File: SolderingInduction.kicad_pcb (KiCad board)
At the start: 4 copper layers, 69 x 37.6 mm, 52 parts, among them J1 MC-307, J3 RBP_GPIO_CONN, SW1 SW_Push, SW2 SW_Push, SW3 SW_Push, SW4 SW_Push, SW5 SW_Push, SW6 SW_Push, SW7 SW_Push, SW8 SW_Push, U1 SPX2920M3-3.3_SOT223, U3 W25Q32JVZP, U4 RP2040, Y1 X322512MMB4SI

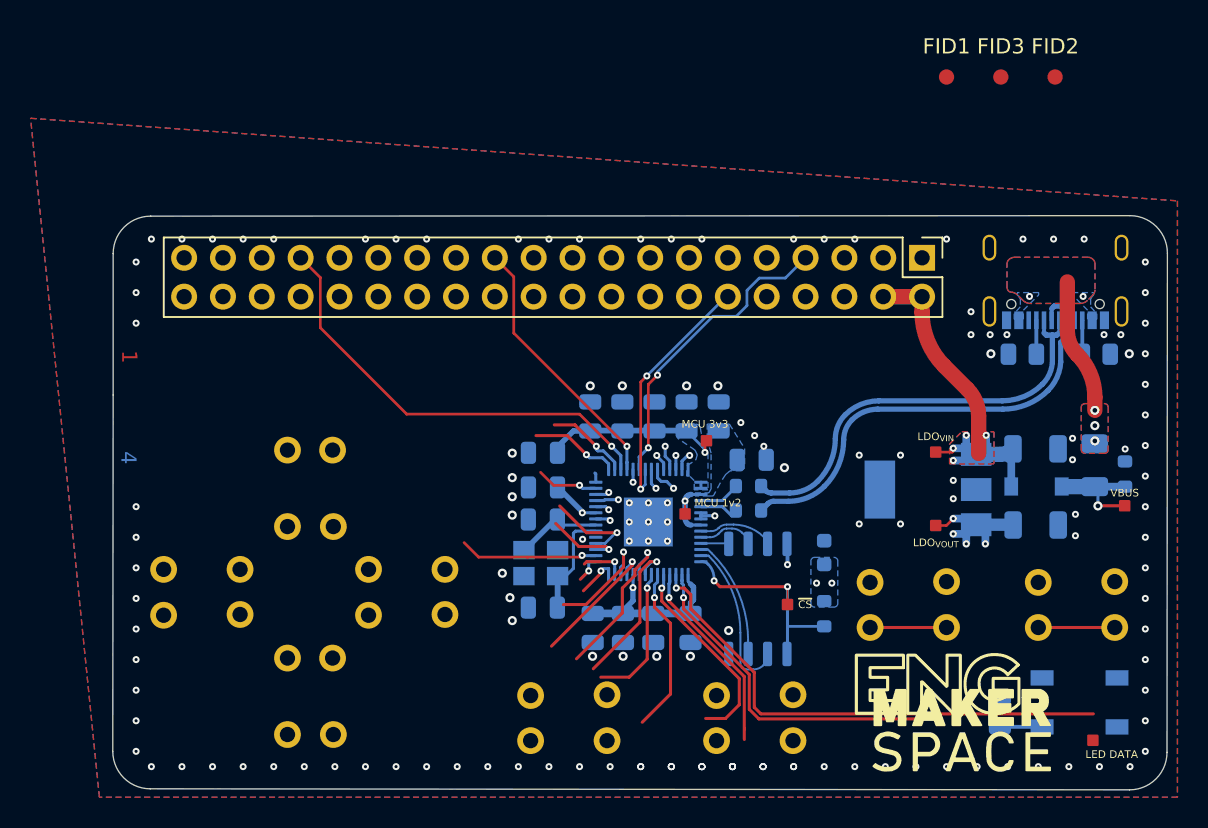
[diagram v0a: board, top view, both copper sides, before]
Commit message: Rough layout run to pinheader
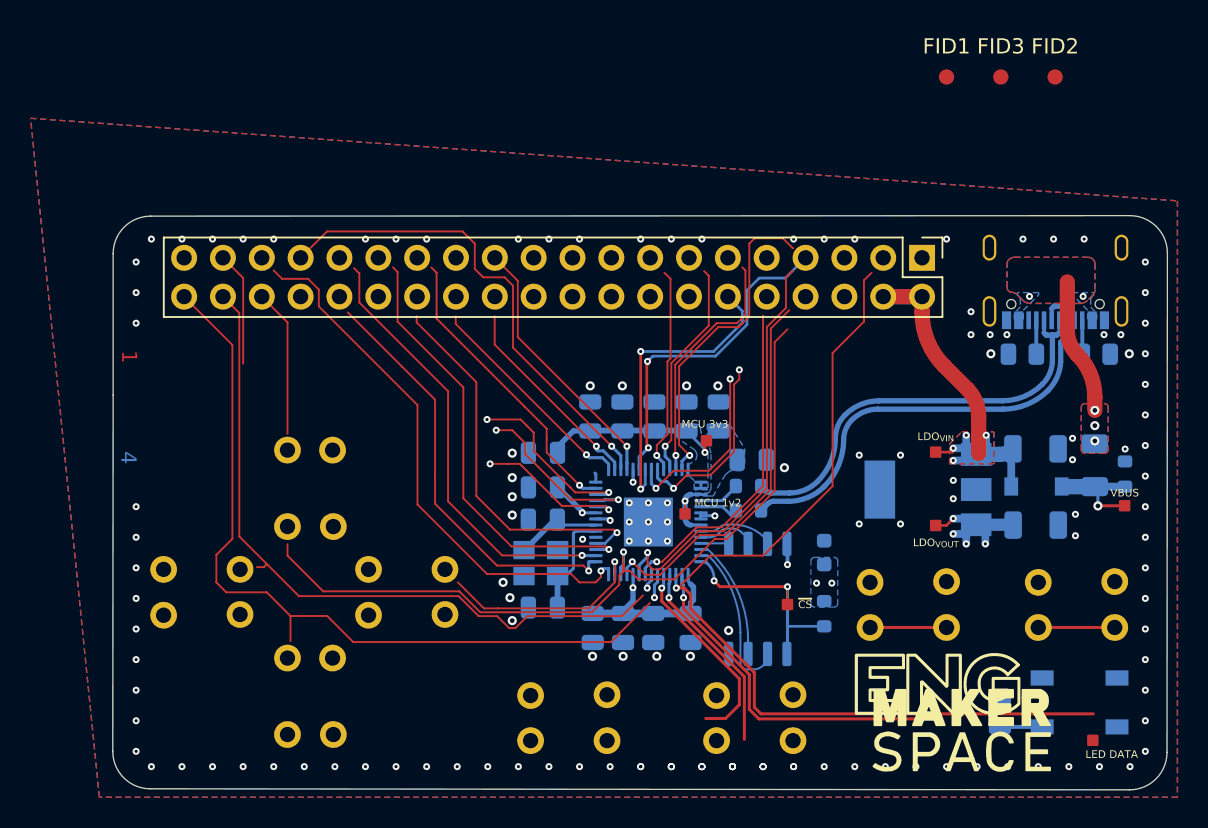
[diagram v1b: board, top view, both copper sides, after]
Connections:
- J3 pad 27: /ID_SDA -> unconnected-(J3-Pad27)
- J3 pad 28: /ID_SCL -> unconnected-(J3-Pad28)
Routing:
- net /$.GPIO24: track 1.36 -> 58.5 mm, vias 1 -> 2
- net /GPIO[21]/PCM.DOUT: track 0.00 -> 53.1 mm
- net /$.GPIO9: track 7.48 -> 52.4 mm
- net /$.GPIO11: track 2.73 -> 35.8 mm
- net /$.GPIO1: track 33.5 -> 61.5 mm
- net /$.GPIO12: track 1.82 -> 27.8 mm
- net /$.GPIO14: track 5.03 -> 28.8 mm
- net /$.GPIO29: track 1.20 -> 21.3 mm
- net /$.GPIO13: track 9.06 -> 28.9 mm
- net /$.GPIO15: track 6.15 -> 25.2 mm
- net /$.GPIO7: track 10.5 -> 27.5 mm
- net /$.GPIO8: track 8.59 -> 24.8 mm
- net /$.GPIO16: track 4.05 -> 19.4 mm
- net /$.GPIO28: track 0.91 -> 16.0 mm
- net /$.GPIO27: track 1.64 -> 14.4 mm
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
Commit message: GPIO/Button fan-out route draft
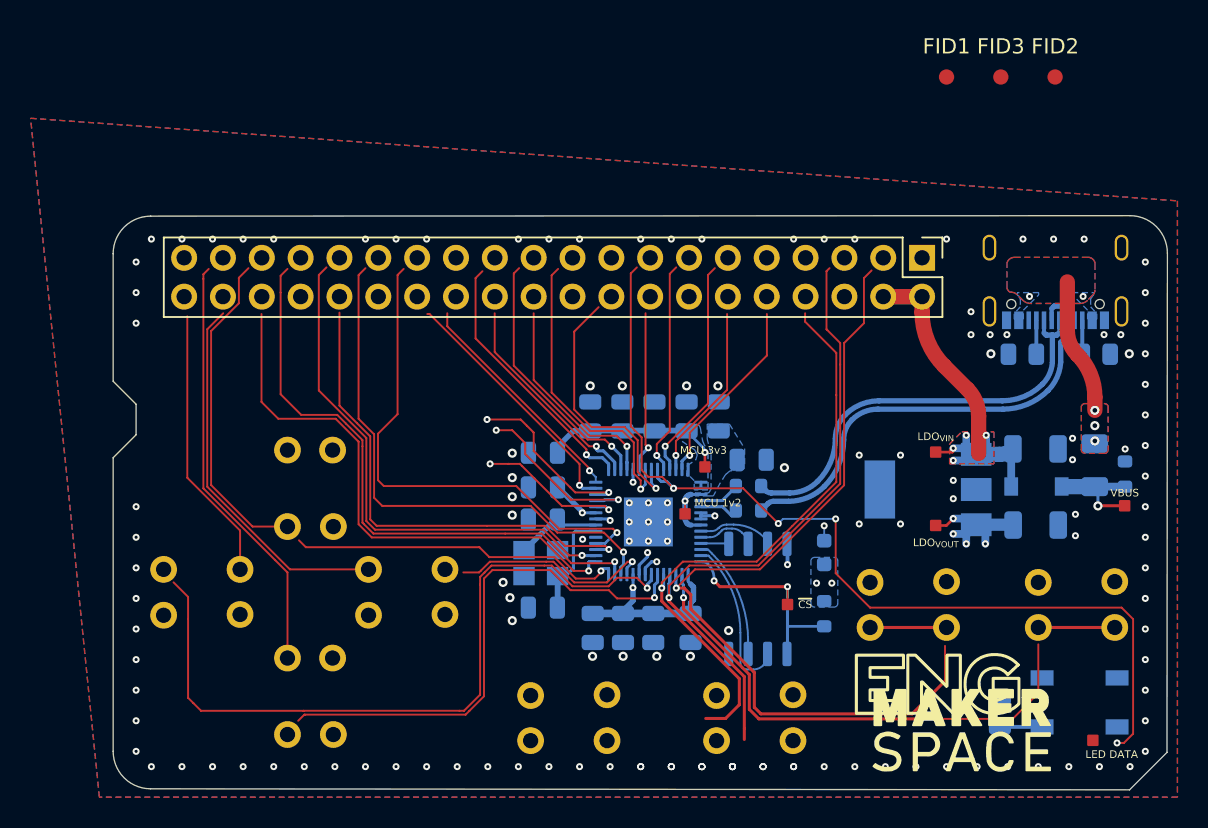
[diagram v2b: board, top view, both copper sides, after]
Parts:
- moved TP1 1.71 mm to (128.7, 71.4)
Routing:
- net /GPIO[21]/PCM.DOUT: track 53.1 -> 0.00 mm
- net /$.GPIO25: track 12.3 -> 62.9 mm, vias 2 -> 4
- net /$.GPIO5: track 1.00 -> 48.8 mm
- net /$.GPIO24: track 58.5 -> 17.4 mm, vias 2 -> 1
- net /$.GPIO4: track 1.60 -> 34.3 mm
- net /$.GPIO2: track 12.8 -> 42.1 mm
- net /BUTTON_LEFT: track 0.00 -> 27.9 mm
- net /$.GPIO3: track 13.2 -> 39.6 mm
- net /$.GPIO7: track 27.5 -> 1.67 mm
- net /$.GPIO10: track 13.8 -> 38.9 mm
- net /BUTTON_A: track 0.00 -> 24.6 mm
- net /BUTTON_SELECT: track 0.00 -> 21.3 mm
- net /$.GPIO6: track 21.5 -> 1.35 mm
- net /BUTTON_DOWN: track 0.00 -> 18.0 mm
- net /$.GPIO9: track 52.4 -> 34.9 mm
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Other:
- board size 69 x 37.6 mm -> 68.9 x 37.6 mm
- board text removed: "1"
- board text removed: "2"
- board text removed: "3"
- board text removed: "4"

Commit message: Cleaned up draft layout of GPIO
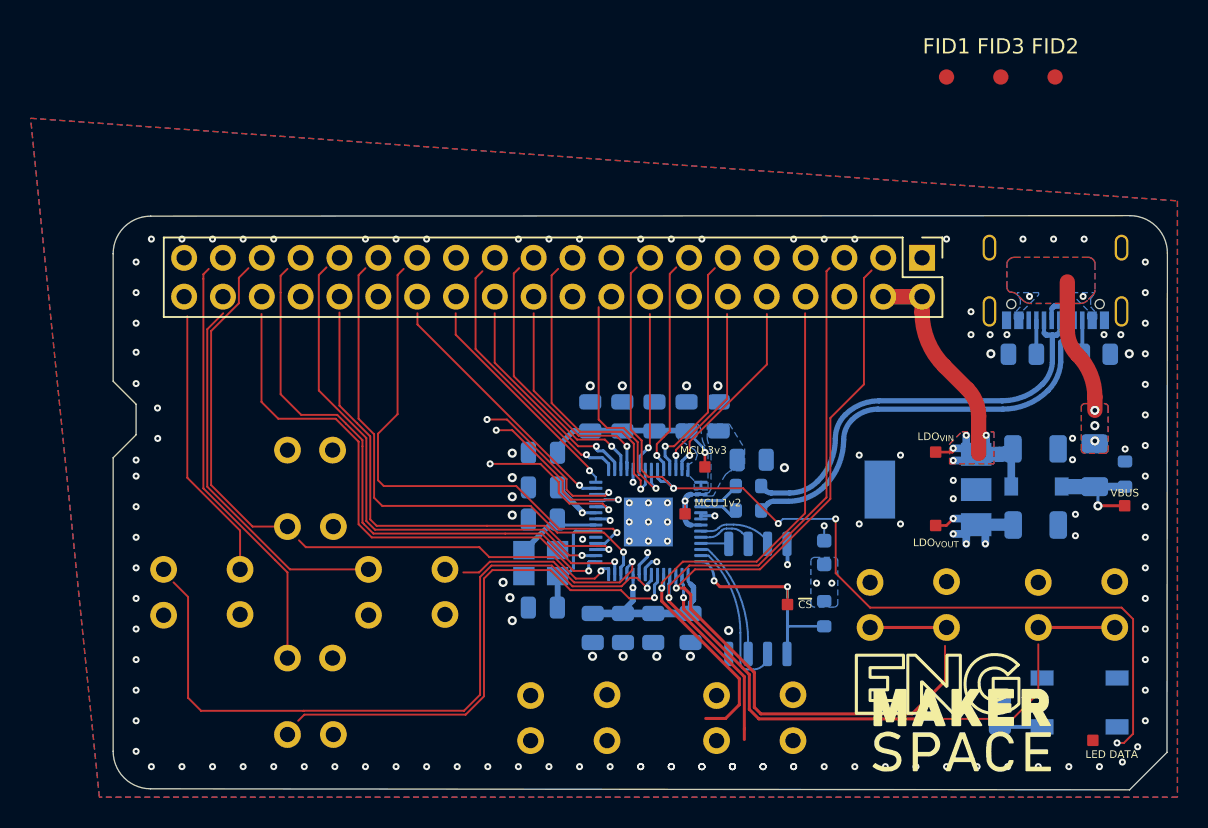
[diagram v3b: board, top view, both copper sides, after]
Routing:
- net /$.GPIO24: track 17.4 -> 15.5 mm
- net /$.GPIO3: track 39.6 -> 37.9 mm
- net /$.GPIO2: track 42.1 -> 41.4 mm
- net GND: vias 142 -> 148
